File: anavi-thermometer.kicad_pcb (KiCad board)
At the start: 2 copper layers, 74.9 x 40.6 mm, 25 parts, among them P1 CONN_01X03, U1 I2C_SENS_1, U2 I2C_SENS_1, U3 I2C_SENS_1

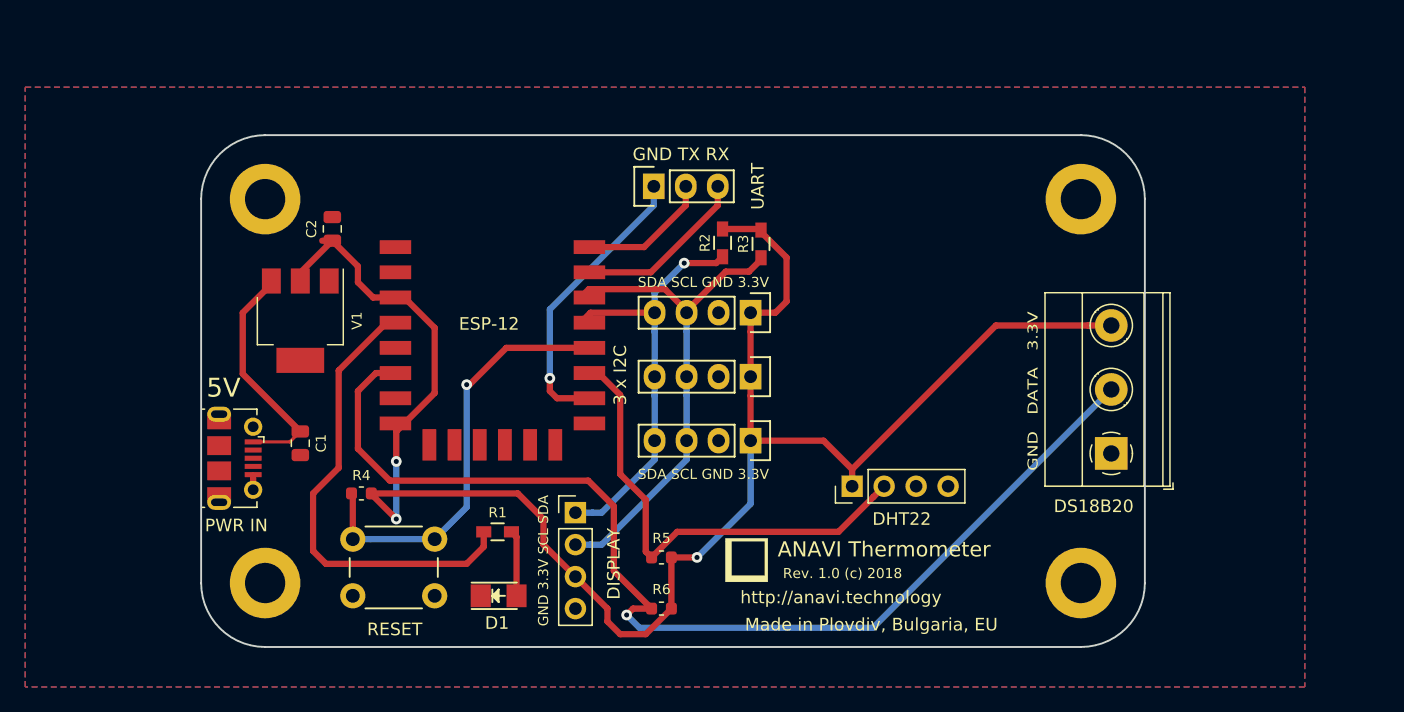
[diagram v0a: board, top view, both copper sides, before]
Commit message: update to Kicad 6
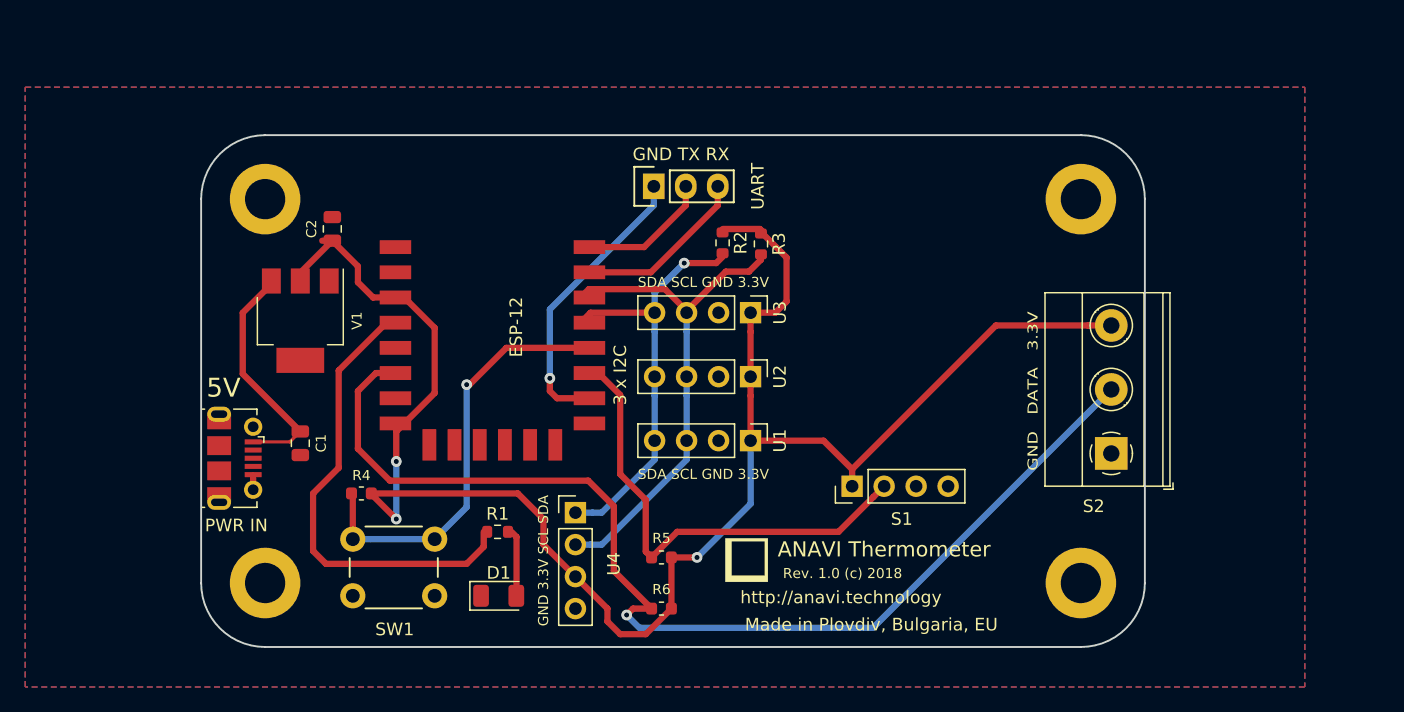
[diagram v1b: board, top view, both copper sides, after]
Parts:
- D1: footprint LEDs:LED_1206 -> LED_SMD:LED_1206_3216Metric
- ESP-12: footprint ESP-12E_SMD -> ESP8266:ESP-12E_SMD
- R1, R2, R3: footprint Resistors_SMD:R_0603_HandSoldering -> Resistor_SMD:R_0603_1608Metric
- S1: renamed from DHT22; value DHT22 -> DHT11
- U1, U2, U3: footprint Pin_Headers:Pin_Header_Straight_1x04 -> Connector_PinHeader_2.54mm:PinHeader_1x04_P2.54mm_Vertical
- renumbered DS18B20 to S2, RESET to SW1, DISPLAY to U4
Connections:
- ESP-12 pad 1: (no net) -> unconnected-(ESP-12-Pad1)
- ESP-12 pad 17: (no net) -> unconnected-(ESP-12-Pad17)
- ESP-12 pad 18: (no net) -> unconnected-(ESP-12-Pad18)
- ESP-12 pad 19: (no net) -> unconnected-(ESP-12-Pad19)
- ESP-12 pad 2: (no net) -> unconnected-(ESP-12-Pad2)
- ESP-12 pad 20: (no net) -> unconnected-(ESP-12-Pad20)
- ESP-12 pad 21: (no net) -> unconnected-(ESP-12-Pad21)
- ESP-12 pad 22: (no net) -> unconnected-(ESP-12-Pad22)
- ESP-12 pad 5: (no net) -> unconnected-(ESP-12-Pad5)
- ESP-12 pad 7: (no net) -> unconnected-(ESP-12-Pad7)
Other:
- net class 12V removed
- net class Default removed
- net class usb removed
- net class vcc removed

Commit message: rev 0.1
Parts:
- removed G***: LOGO, logo:anavi-logo
- removed PWR IN: USB_B_Micro, Connector_USB:USB_Micro-B_Molex-105017-0001
- removed R6: 4,7K, Resistor_SMD:R_0603_1608Metric
- removed REF** (x4): MountingHole_3.2mm_M3_DIN965_Pad, Mounting_Holes:MountingHole_3.2mm_M3_DIN965_Pad
- removed S2: DS18B20, TerminalBlock_Phoenix:TerminalBlock_Phoenix_MKDS-1,5-3-5.08_1x03_P5.08mm_Horizontal
- removed U1, U2, U3: I2C_SENS_1, Connector_PinHeader_2.54mm:PinHeader_1x04_P2.54mm_Vertical
- added J1: USB_A, GCT_USB1061_Horizontal:USB_A_Plug_GCT_USB1061_Horizontal, F.Cu at (140.0, 80.0)
- C1, C2, ESP-12, R2, R3, R4, R5, V1: moved to B.Cu
- U4: value Conn_01x04 -> SSD1306; footprint Connector_PinHeader_2.54mm:PinHeader_1x04_P2.54mm_Vertical -> SSD1306:128x64OLED
- moved V1 81.5 mm to (154.0, 91.0)
- moved C1 81.0 mm to (153.0, 85.0), turned to 180 degrees
- moved C2 79.0 mm to (152.0, 97.0), turned to 180 degrees
- moved ESP-12 61.0 mm to (133.4, 111.1)
- moved P1 55.4 mm to (155.8, 81.6), turned to -90 degrees
- moved R4 51.4 mm to (128.0, 109.0), turned to 90 degrees
- moved SW1 49.7 mm to (123.8, 78.8), turned to 0 degrees
- moved U4 45.6 mm to (140.0, 97.8)
- moved R2 42.9 mm to (148.5, 86.3)
- moved R3 37.9 mm to (146.6, 86.3)
- moved R1 35.7 mm to (124.0, 103.0), turned to -90 degrees
- moved D1 35.7 mm to (124.0, 110.0), turned to 90 degrees
- moved R5 33.5 mm to (132.0, 91.2), turned to -90 degrees
- moved S1 12.5 mm to (124.0, 89.0), turned to 0 degrees
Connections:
- ESP-12 pad 6: Net-(ESP-12-Pad6) -> unconnected-(ESP-12-Pad6)
- U4 pad 1: Net-(ESP-12-Pad13) -> GND
- U4 pad 2: Net-(ESP-12-Pad14) -> +3V3
- U4 pad 3: +3V3 -> Net-(ESP-12-Pad14)
- U4 pad 4: GND -> Net-(ESP-12-Pad13)
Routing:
- net Net-(ESP-12-Pad6): track 89.4 -> 0.00 mm, vias 1 -> 0
- net GND: track 23.5 -> 108.2 mm
- net +3V3: track 143.2 -> 78.8 mm, vias 3 -> 0
- net Net-(ESP-12-Pad16): track 11.2 -> 39.7 mm, vias 0 -> 1
- net Net-(ESP-12-Pad4): track 37.7 -> 10.8 mm, vias 0 -> 1
- net Net-(ESP-12-Pad15): track 14.6 -> 38.3 mm, vias 0 -> 1
- net Net-(ESP-12-Pad12): track 33.7 -> 53.1 mm, vias 2 -> 4
- net unconnected-(J1-Pad5): track 0.00 -> 14.7 mm
- net Net-(ESP-12-Pad11): track 38.6 -> 28.6 mm, vias 0 -> 2
- net Net-(ESP-12-Pad13): track 34.4 -> 27.9 mm, vias 1 -> 2
- net Net-(ESP-12-Pad14): track 40.6 -> 35.0 mm, vias 0 -> 1
- net +5V: track 19.4 -> 18.5 mm, vias 0 -> 1
- removed copper zone on B.Cu, net GND
- removed copper zone on F.Cu, net GND
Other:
- board size 74.9 x 40.6 mm -> 36 x 36 mm
- board text added: "2022-01-08 rev 0.1"
- board text added: "3V3"
- board text added: "DAT"
- board text added: "GND"
- board text added: "NC"
- board text added: "SDA SCL 3.3V GND"
- board text added: "based on Anavi thermometer"
- board text removed: "3 x I2C"
- board text removed: "5V"
- board text removed: "ANAVI Thermometer"
- board text removed: "GND 3.3V SCL SDA"
- board text removed: "GND DATA 3.3V"
- board text removed: "Made in Plovdiv, Bulgaria, EU"
- board text removed: "Rev. 1.0 (c) 2018"
- board text removed: "SDA SCL GND 3.3V"
- board text removed: "UART"
- board text removed: "http://anavi.technology"
